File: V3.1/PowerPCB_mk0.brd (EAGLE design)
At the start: 171.9 x 151.6 mm, 124 parts, among them CON1 PINHEAD_1X12-2.54-FEMALE, CON2 PINHEAD_1X06-2.54-FEMALE, CON3 PINHEAD_1X02-2.54-FEMALE, CON4 PINHEAD_1X06-2.54-FEMALE, CON7 PINHEAD_1X06-2.54-FEMALE, IC1 TPS54560B, IC10 TPS54260, IC2 TPS54560B, IC3 TPS54560B, IC4 TPS54560B, IC5 INA169, J1 CONNECTION-7MM, M1 BATTERY_CON-XT30-RA, M2 BATTERY_CON-XT30-RA, M3 BATTERY_CON-XT30-RA, M4 BATTERY_CON-XT30-RA, M5 BATTERY_CON-XT30-RA, M6 BATTERY_CON-XT30-RA, M7 BATTERY_CON-XT30-RA, Q1 IRFR2407PBF, Q2 IRFR2407PBF, Q3 IRFR2407PBF

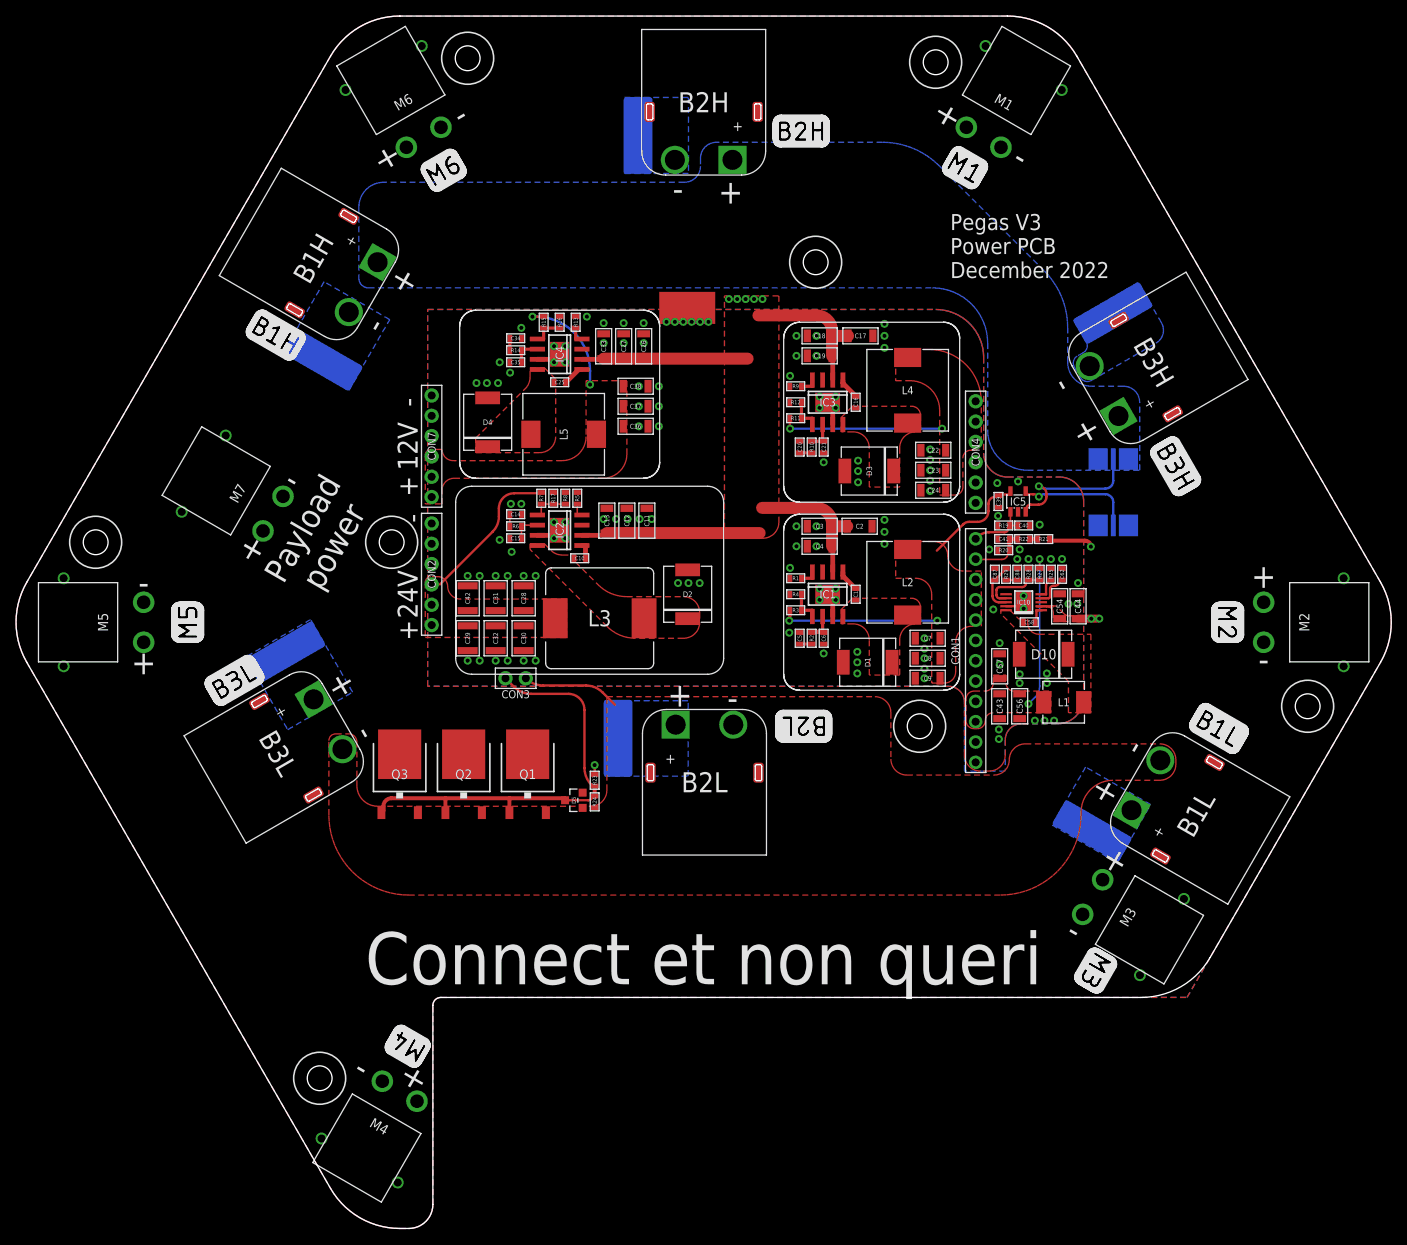
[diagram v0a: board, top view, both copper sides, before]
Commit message: InterPCB connectors issues fix
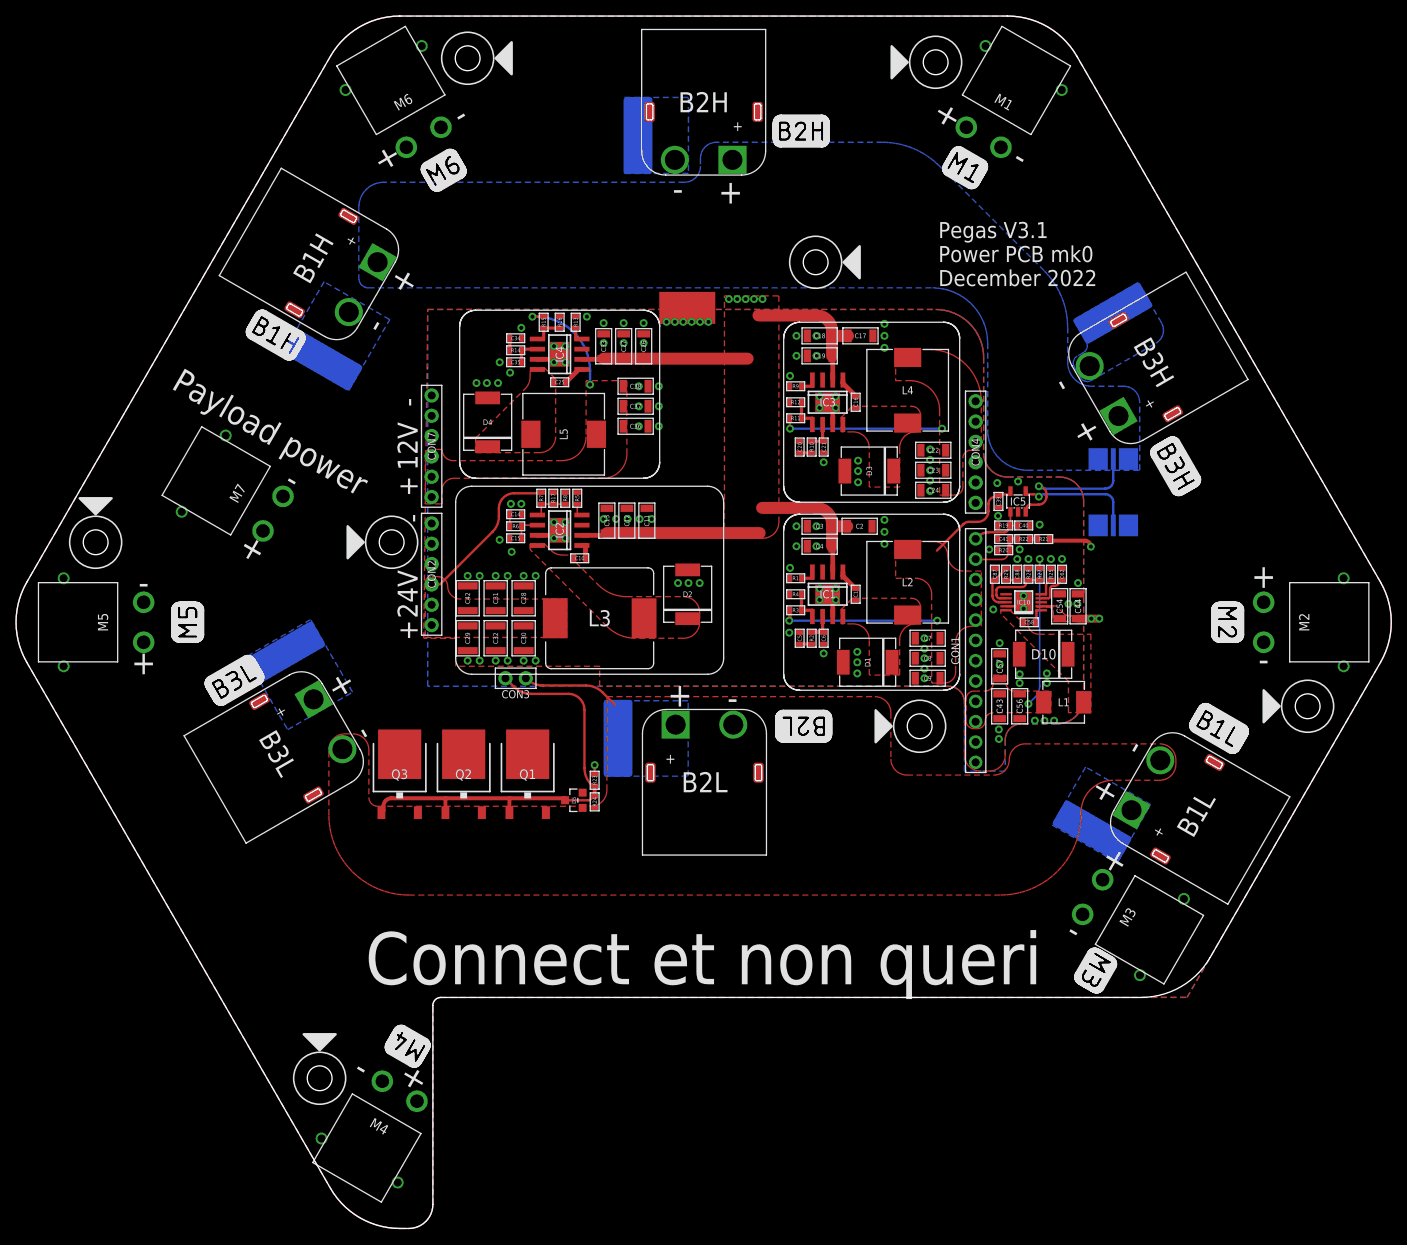
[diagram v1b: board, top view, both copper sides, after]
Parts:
- R27: value 143K -> 39K
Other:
- board text added: "Pegas V3.1 Power PCB mk0 December 2022"
- board text removed: "Pegas V3 Power PCB December 2022"

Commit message: silk updates
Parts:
- added C45: 4700p, rc:C0603
- C39: value 0.1uF -> 0.1u
- C62: value 10n -> 4700p
- R20, R23: value 10K2 -> 10K
- moved CON3 9.51 mm to (-14.0, -7.50)
- moved CON7 2.00 mm to (-34.0, 24.0)
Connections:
- net GND: now also C45.2
- net N$20: now also C45.1
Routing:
- net PWRSW: track 54.4 -> 46.7 mm
- net BATNEG: track 12.1 -> 5.94 mm
- net N$20: track 4.07 -> 5.47 mm

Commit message: Minor fixes here and there
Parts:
- removed R19: 82K, rc:R0603
- added D11, D12, D13, D6, D7, D8, D9: SMBJ51CA-SMB, TVS_diodes:DO-214AA(SMB)
- added R26: 700 µOhms, SHUNT_RESISTORS:R3920-KELVIN
- added RL: 53K6, rc:R0603
- added RL1: DNM, rc:R0603
- R18: value 200 µOhms -> 700 µOhms
- R21: value 82K -> 143K
- R22: value 82K -> 18K
- moved C39 0.98 mm to (37.8, 15.5)
- moved IC5 0.92 mm to (40.2, 14.9)
- moved M4 0.62 mm to (-38.0, -58.0)
- moved M7 0.46 mm to (-54.0, 14.0)
- moved M3 0.20 mm to (48.5, -34.5)
- moved M6 0.12 mm to (-35.0, 60.5)
- moved M1 0.12 mm to (35.0, 60.5)
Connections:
- net BATT_CURRENT: now also RL.2, RL1.2; no longer R19.2
- net GND: now also RL.1, RL1.1; no longer R19.1
- net N$19: now also R26.S2
- net N$21: now also R26.S1
- net PGND: now also D11.A, D12.A, D13.A, D6.A, D7.A, D8.A, D9.A
- net VBAT: now also D11.C, D12.C, D13.C, D6.C, D7.C, D8.C, D9.C, R26.2, R26.22
- net VDC: now also R26.1, R26.11
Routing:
- net VBAT: track 90.9 -> 115.9 mm
- net N$21: track 17.7 -> 27.8 mm
- net N$19: track 14.8 -> 24.1 mm
- net BATT_CURRENT: track 7.78 -> 8.68 mm
- net 5VFMU: track 32.9 -> 33.6 mm
- net GND: vias 127 -> 126
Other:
- board text added: "25 mm"
- board text added: "Apply heatsink here if needed"
- board text added: "Use 11 mm M3 male to female PCB standoffs between the PCBs"

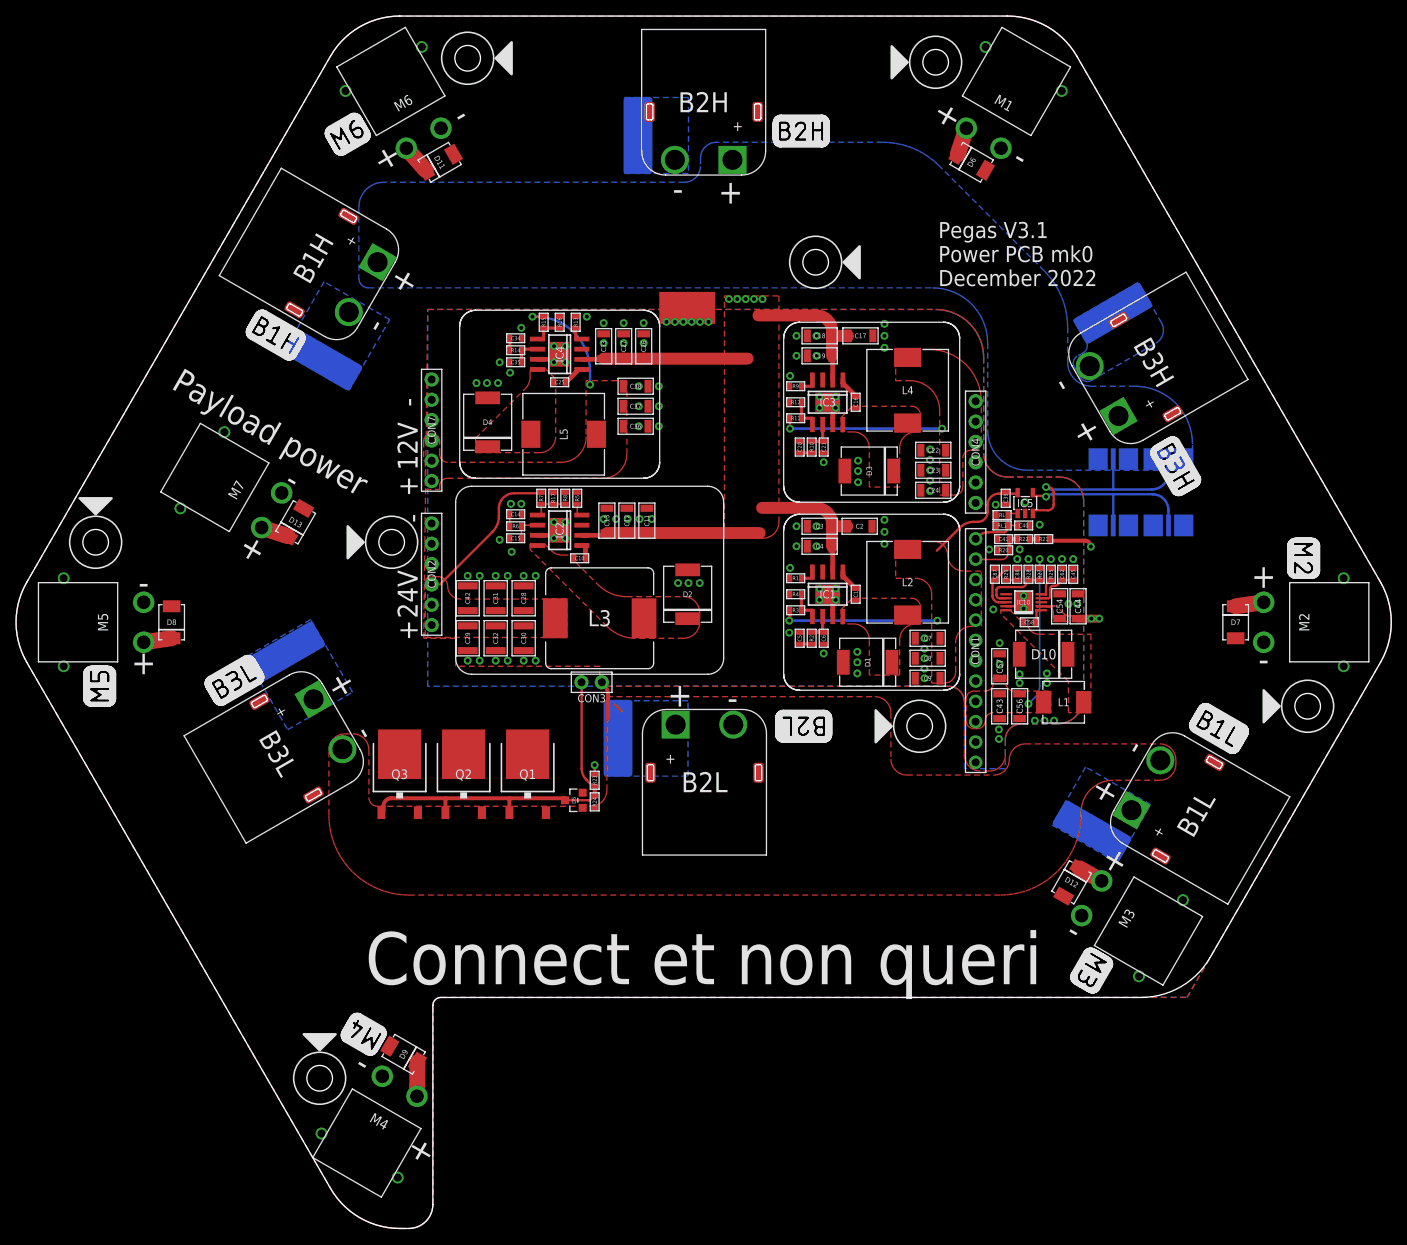
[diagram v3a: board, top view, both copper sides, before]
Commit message: PowerPCB updated for compatibility with rezonit requerements
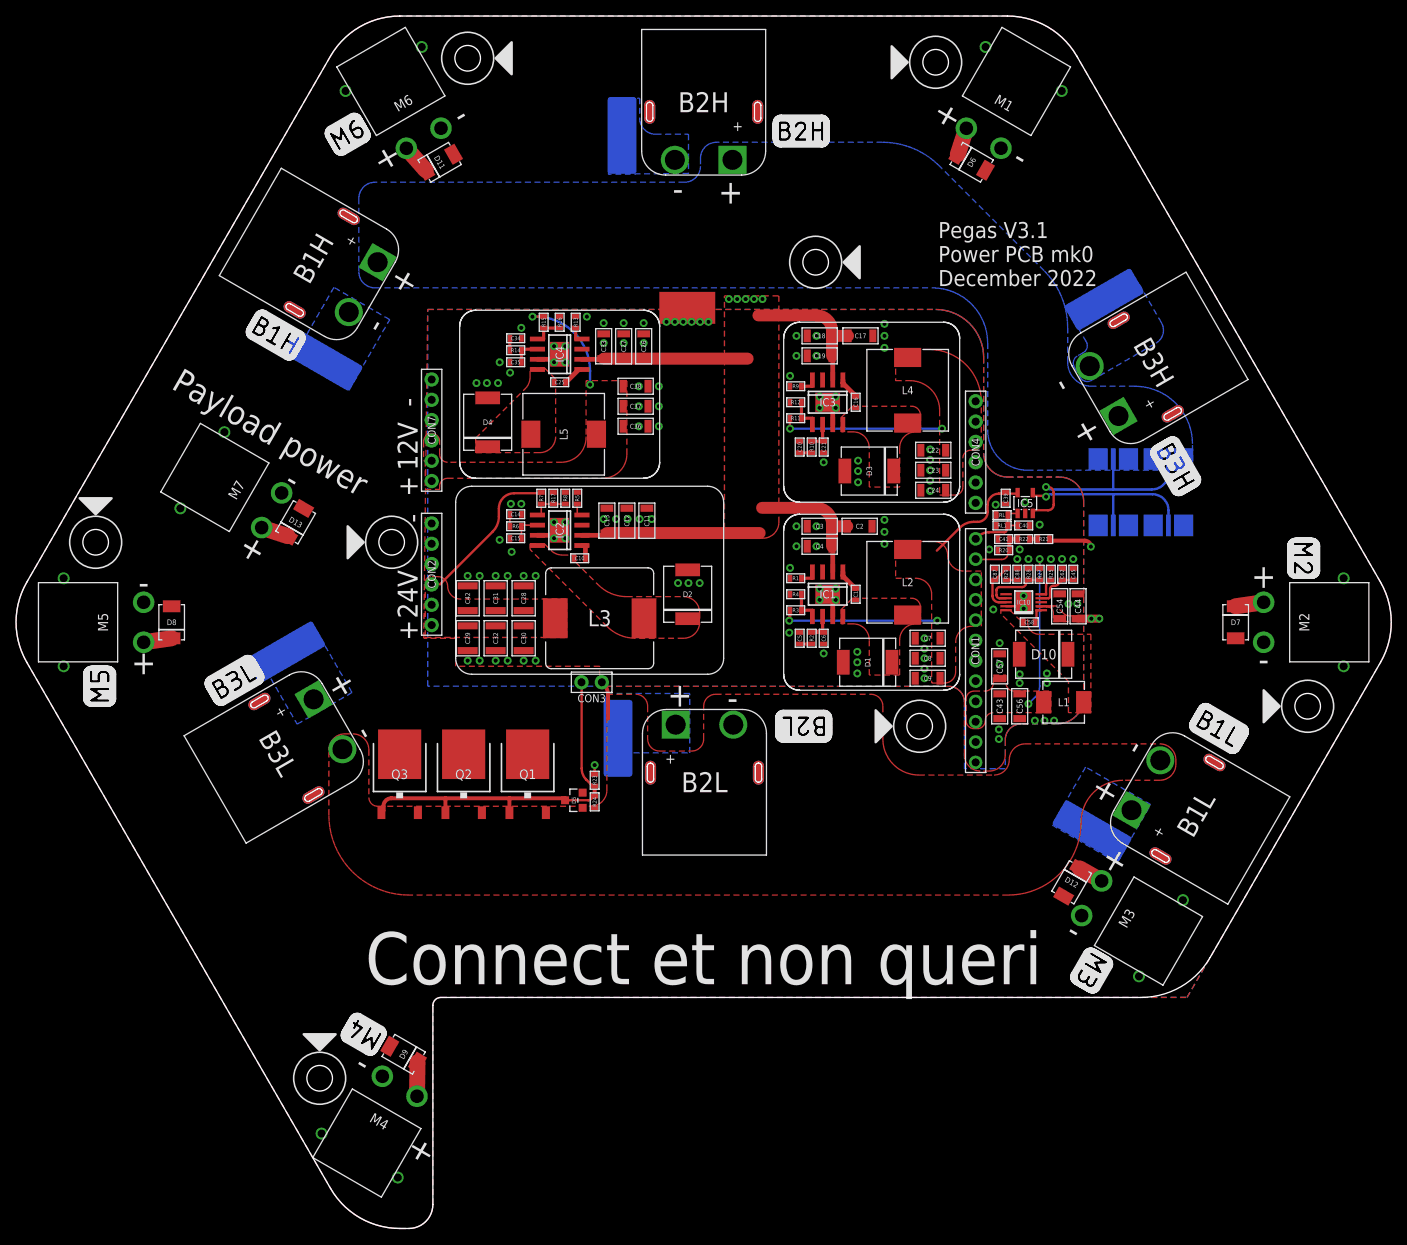
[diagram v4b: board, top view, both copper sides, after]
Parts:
- moved PAD2 2.02 mm to (50.0, 40.4)
- moved PAD5 2.00 mm to (-10.2, 60.9)
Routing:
- net BATNEG: track 5.94 -> 4.75 mm
